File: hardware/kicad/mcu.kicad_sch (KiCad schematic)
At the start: 0 parts

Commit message: kicad: chunk #4 - MCU sub-sheet (ESP32-C6 SuperMini)
Populates mcu.kicad_sch with the ESP32-C6 SuperMini module
connector (U3), local 3.3V decoupling (C9 10uF + C9b 100nF),
and an unpopulated SWD/UART recovery header (J2, DNP).

ESP32-C6 SuperMini chosen per v0.3 research: lowest average
WiFi-active current (~60mA) thanks to WiFi 6 TWT/OFDMA, 512KB
SRAM headroom for BLE-proxy, ESPHome 2026 standardized on C6
for BLE-proxy roles. Antenna edge points to 12:00 (case wall)
per the clock-face sector layout.

Pinout (per v0.3 ARCHITECTURE.md, post strap-pin verification):
- GPIO 6 / 7: I2C SDA / SCL (shared bus, SEN66 + VEML7700 + NFC)
- GPIO 16 / 17: UART TX / RX (to LD2410 @ 256000 baud)
- GPIO 10: LD2410 OUT presence interrupt (was GPIO 4 - MTMS strap)
- GPIO 11: NFC FD interrupt (was GPIO 5 - MTDI strap)
- GPIO 8: onboard WS2812 status LED (no external WS2812 in v1)
- EN, GPIO 9: exposed on J2 recovery header

No external USB-C connector - flashing uses the SuperMini's own
onboard USB-C accessible before the enclosure is sealed. OTA via
ESPHome+HA handles all post-deployment updates.

J2 (SWD/UART recovery header, 6 pins) is marked DNP - footprint
exists on PCB for emergency hand-soldering if OTA fails, but is
not assembled by default.

Inter-sheet signals (I2C, UART, presence / NFC interrupts) are
exposed as hierarchical labels in mcu.kicad_sch and matching
sheet ports were preemptively added to oas.kicad_sch's MCU
sheet block, ready for the sensors sub-sheet (chunk #5).

Generator changes:
- New SUBSHEET_PINS dict + _gen_sheet_pin helper: declarative
  sheet port specification on the root sheet block.
- _gen_sheet_block rewritten without textwrap.dedent so the
  interpolated pin_block does not corrupt the leading whitespace
  pattern (fixes an indentation bug).
- _sch_capacitor and _sch_power_flag gained a sheet_key parameter
  (defaults to "power") so they can record the correct hierarchy
  path in their (instances ...) block when called from gen_mcu_sch.
- New hel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
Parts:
- added C9: 10uF 10V, symbol Device:C_Polarized
- added C9b: 100nF, symbol Device:C
- added J2: SWD/UART Recovery (DNP), symbol Connector_Generic:Conn_01x06
- added U3: ESP32-C6 SuperMini, symbol OAS:ESP32-C6_SuperMini
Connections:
- new net: J2.4 (Pin_4), U3.10 (GPIO9)
- new net: J2.3 (Pin_3), U3.9 (EN)
- new net +3V3: C9.1, C9b.1, J2.1 (Pin_1), U3.3 (3V3)
- new net GND: C9.2, C9b.2, J2.2 (Pin_2), U3.2 (GND)
- new net I2C_SCL: U3.5 (GPIO7)
- new net I2C_SDA: U3.4 (GPIO6)
- new net LD2410_OUT: U3.7 (GPIO10)
- new net NFC_FD: U3.8 (GPIO11)
- new net UART_RX: J2.6 (Pin_6), U3.12 (GPIO17)
- new net UART_TX: J2.5 (Pin_5), U3.11 (GPIO16)
- no-connect marks 0 -> 6

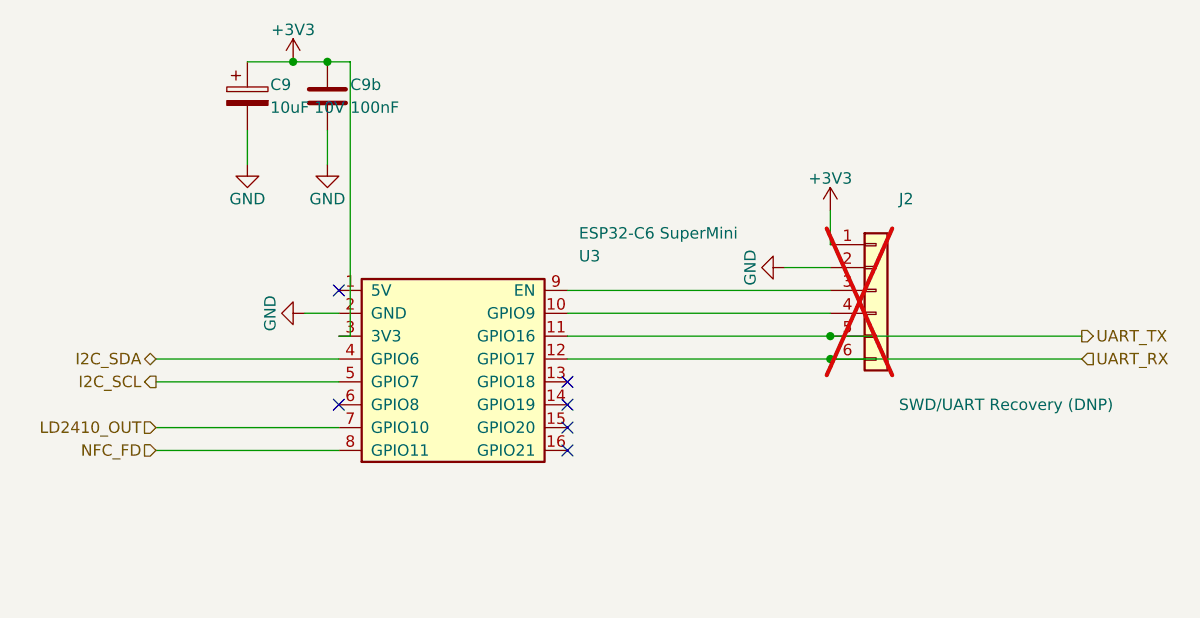
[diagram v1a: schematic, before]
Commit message: kicad: chunk #4 fix - J2 recovery header pinout (all 6 signals)
Fixes a layout bug in commit 2e83a5b: J2 (SWD/UART recovery,
DNP) had pin 1 left unconnected and the UART_RX wire passed
2.54 mm below J2 pin 6 without actually tapping into the
connector. A dangling junction at (194.31, 109.22) marked
where UART_RX should have entered but didn't. Net effect:
the recovery header was missing UART_RX, making it useless
for actual recovery flashing.

Refactored gen_mcu_sch() to map all 6 required recovery
signals into J2:
- Pin 1: +3V3   (programmer supplies power if needed)
- Pin 2: GND
- Pin 3: UART_TX (GPIO16)
- Pin 4: UART_RX (GPIO17)
- Pin 5: EN (reset)
- Pin 6: GPIO9 (BOOT mode)

Removed the dangling junction. No topology change in any
electrical net - all signals exist as before, only J2's
tapping points moved.

ERC and DRC unchanged. Generation deterministic.

Co-Authored-By: Claude Opus 4.7 (1M context) <noreply@anthropic.com>
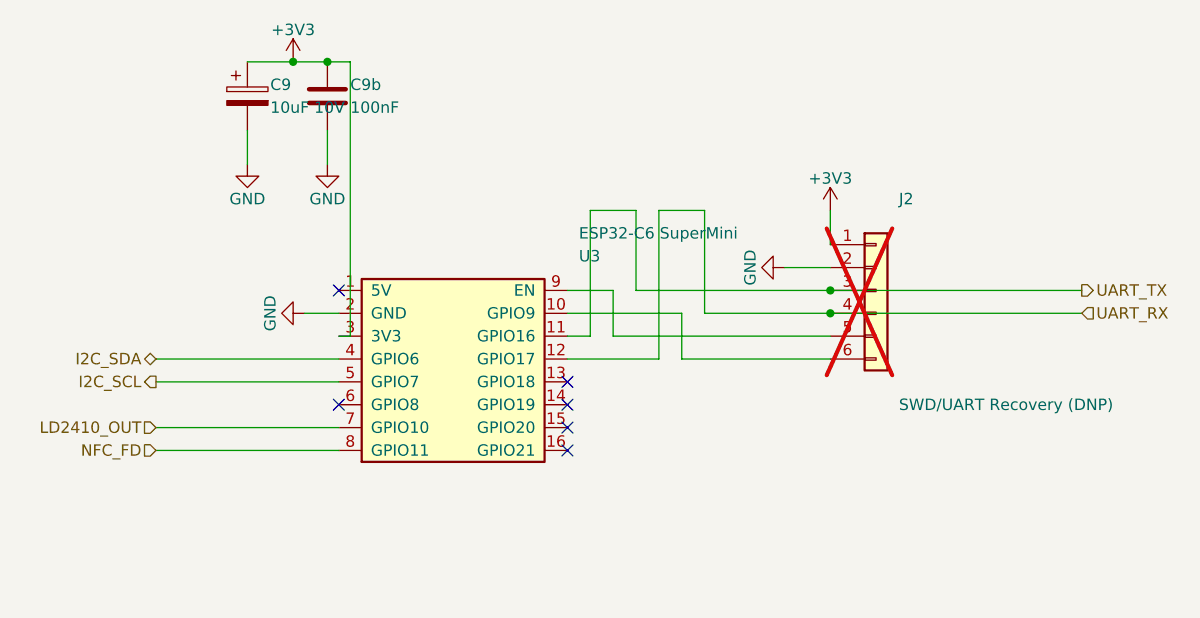
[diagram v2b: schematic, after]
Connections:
- net UART_RX: now also J2.4 (Pin_4); no longer J2.6 (Pin_6)
- net UART_TX: now also J2.3 (Pin_3); no longer J2.5 (Pin_5)
- net at U3.10 (GPIO9): now also J2.6 (Pin_6); no longer J2.4 (Pin_4)
- net at U3.9 (EN): now also J2.5 (Pin_5); no longer J2.3 (Pin_3)
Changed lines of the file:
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@@
 (wire
 	(pts
-		(xy 165.1 101.6) (xy 194.31 101.6)
-	)
-	(stroke
-		(width 0)
-		(type default)
-	)
-)
-(wire
-	(pts
-		(xy 165.1 104.14) (xy 194.31 104.14)
-	)
-	(stroke
-		(width 0)
-		(type default)
-	)
-)
-(wire
-	(pts
-		(xy 165.1 106.68) (xy 222.25 106.68)
-	)
-	(stroke
-		(width 0)
-		(type default)
-	)
-)
-(wire
-	(pts
-		(xy 165.1 109.22) (xy 222.25 109.22)
+		(xy 165.1 101.6) (xy 170.18 101.6)
+	)
+	(stroke
+		(width 0)
+		(type default)
+	)
+)
+(wire
+	(pts
+		(xy 170.18 101.6) (xy 170.18 106.68)
+	)
+	(stroke
+		(width 0)
+		(type default)
+	)
+)
+(wire
+	(pts
+		(xy 170.18 106.68) (xy 194.31 106.68)
+	)
+	(stroke
+		(width 0)
+		(type default)
+	)
+)
+(wire
+	(pts
+		(xy 165.1 104.14) (xy 177.8 104.14)
+	)
+	(stroke
+		(width 0)
+		(type default)
+	)
+)
+(wire
+	(pts
+		(xy 177.8 104.14) (xy 177.8 109.22)
+	)
+	(stroke
+		(width 0)
+		(type default)
+	)
+)
+(wire
+	(pts
+		(xy 177.8 109.22) (xy 194.31 109.22)
+	)
+	(stroke
+		(width 0)
+		(type default)
+	)
+)
+(wire
+	(pts
+		(xy 165.1 106.68) (xy 167.64 106.68)
+	)
+	(stroke
+		(width 0)
+		(type default)
+	)
+)
+(wire
+	(pts
+		(xy 167.64 106.68) (xy 167.64 92.71)
+	)
+	(stroke
+		(width 0)
+		(type default)
+	)
+)
+(wire
+	(pts
+		(xy 167.64 92.71) (xy 172.72 92.71)
+	)
+	(stroke
+		(width 0)
+		(type default)
+	)
+)
+(wire
+	(pts
+		(xy 172.72 92.71) (xy 172.72 101.6)
+	)
+	(stroke
+		(width 0)
+		(type default)
+	)
+)
+(wire
+	(pts
+		(xy 172.72 101.6) (xy 222.25 101.6)
 	)
 	(stroke
@@
 )
 (junction
-	(at 194.31 106.68)
+	(at 194.31 101.6)
 	(diameter 0)
 	(color 0 0 0 0)
 )
+(wire
+	(pts
+		(xy 165.1 109.22) (xy 175.26 109.22)
+	)
+	(stroke
+		(width 0)
+		(type default)
+	)
+)
+(wire
+	(pts
+		(xy 175.26 109.22) (xy 175.26 92.71)
+	)
+	(stroke
+		(width 0)
+		(type default)
+	)
+)
+(wire
+	(pts
+		(xy 175.26 92.71) (xy 180.34 92.71)
+	)
+	(stroke
+		(width 0)
+		(type default)
+	)
+)
+(wire
+	(pts
+		(xy 180.34 92.71) (xy 180.34 104.14)
+	)
+	(stroke
+		(width 0)
+		(type default)
+	)
+)
+(wire
+	(pts
+		(xy 180.34 104.14) (xy 222.25 104.14)
+	)
+	(stroke
+		(width 0)
+		(type default)
+	)
+)
 (junction
-	(at 194.31 109.22)
+	(at 194.31 104.14)
 	(diameter 0)
 	(color 0 0 0 0)
@@
 (hierarchical_label "UART_TX"
 	(shape output)
-	(at 222.25 106.68 0)
+	(at 222.25 101.6 0)
 	(effects
 		(font
@@
 (hierarchical_label "UART_RX"
 	(shape input)
-	(at 222.25 109.22 0)
-	(effects
-		(font
+	(at 222.25 104.14 0)
+	(effects
+		(font

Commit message: kicad: chunk #4 fix - v0.4 pinout + I2C pullups + DevKitM-1 symbol rebuild
Replace the OAS:ESP32-C6_SuperMini custom symbol (modeled on a generic 2x8
SIP, 16 pins) with OAS:ESP32-C6_DevKitM-1, built from the Espressif official
user guide pin layout (2x15 SIP, 30 pins total, J1 left + J3 right). Symbol
description carries MPN, EAN, datasheet URL, and chip-level notes (SiP flash,
GPIO 10/11 not bonded, 22 GPIOs available).

Apply the v0.4 signal-routing corrections:
  * LD2410_OUT: GPIO 10 (does not exist on SiP flash) -> GPIO 2 (safe input)
  * NFC_FD:    GPIO 11 (does not exist on SiP flash) -> GPIO 3 (safe input)

Add the I2C pullups flagged HIGH by the chunk #4 review:
  * R5: 4.7k 1% 0402, SDA -> +3V3
  * R6: 4.7k 1% 0402, SCL -> +3V3
Both placed near U3.10/U3.11 (GPIO 6/7) where the bus originates.

Bump C9 from 10V to 16V (0402 derating margin per review feedback). C9b
(100nF decoupling) unchanged.

Single-source-of-truth pin tables: ESP32C6_DEVKITM1_PINS (30 entries),
ESP32C6_DEVKITM1_SIGNAL_PIN (OAS-signal -> pin number lookup), and
ESP32C6_DEVKITM1_NC_PINS (no-connect list). Helpers _esp32c6_devkitm1_
lib_symbol() and _mcu_pin_xy() consume these tables so the schematic
mirrors the typed data — any future pinout change is a one-edit fix.

_sch_resistor() now takes a sheet_key parameter (default "power") so the
MCU sheet can pass "mcu" for its pullups. _sch_local_label() added for
short cross-body labels (RST, BOOT) connecting U3 to recovery header J2.

Determinism verified: two consecutive python generate.py runs produce
bit-identical mcu.kicad_sch (md5 d9e8810d7d465f22a01b8bd12c89970c).

DRC: 0 violations. ERC: 9 messages (6 errors + 3 warnings) -- all expected
incremental-build artifacts (hier labels I2C_SDA/SCL/LD2410_OUT/NFC_FD/
UART_TX/UART_RX waiting for sensors.kicad_sch and io.kicad_sch sheets to
declare matching pins). Two warnings dropped vs v0.5 baseline because the
I2C pullups now give SDA/SCL a second connection point on the MCU sheet.

Co-Author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
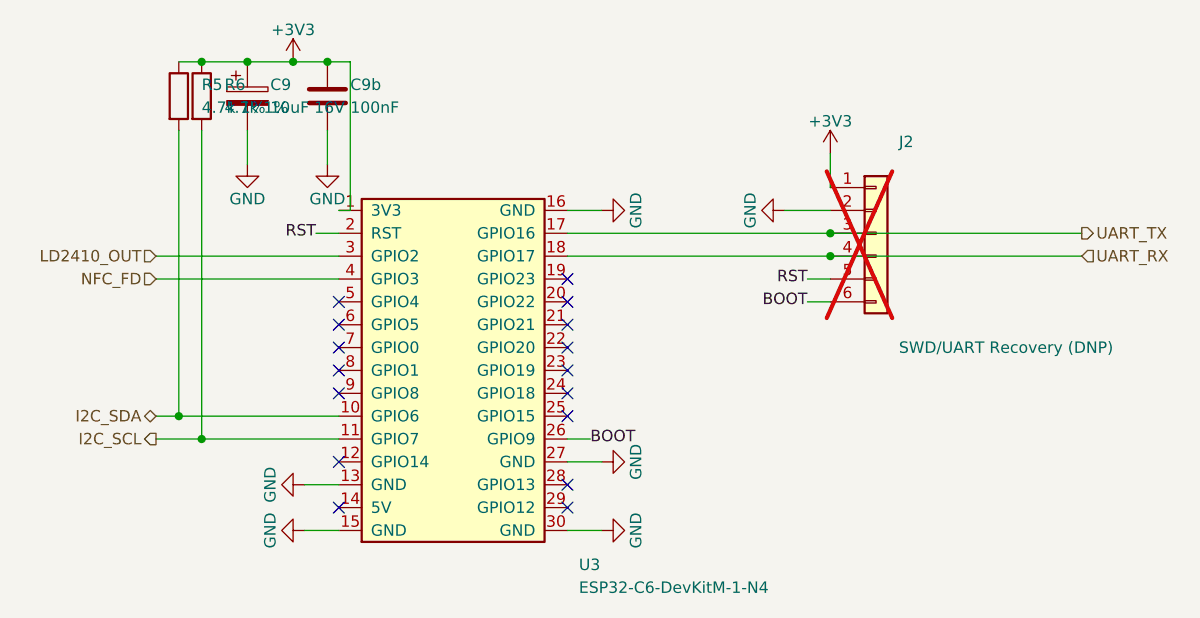
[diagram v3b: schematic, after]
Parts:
- removed U3: ESP32-C6 SuperMini, symbol OAS:ESP32-C6_SuperMini
- added R5, R6: 4.7k 1%, symbol Device:R
- added U3: ESP32-C6-DevKitM-1-N4, symbol OAS:ESP32-C6_DevKitM-1
- C9: value 10uF 10V -> 10uF 16V
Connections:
- net +3V3: now also R5.1, R6.1, U3.1 (3V3)
- net GND: now also U3.13 (GND), U3.15 (GND), U3.16 (GND), U3.27 (GND), U3.30 (GND)
- net I2C_SCL: now also R6.2, U3.11 (GPIO7)
- net I2C_SDA: now also R5.2, U3.10 (GPIO6)
- net LD2410_OUT: now also U3.3 (GPIO2)
- net NFC_FD: now also U3.4 (GPIO3)
- net UART_RX: now also U3.18 (GPIO17)
- net UART_TX: now also U3.17 (GPIO16)
- net BOOT: now reaches J2.6 (Pin_6)
- net BOOT: now also U3.26 (GPIO9)
- net RST: now reaches J2.5 (Pin_5)
- net RST: now also U3.2 (RST)
- no-connect marks 6 -> 16

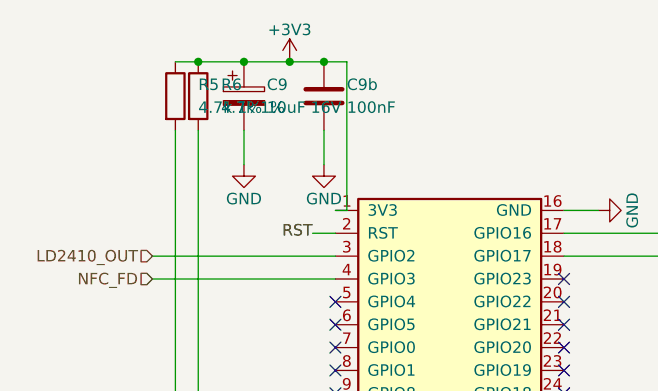
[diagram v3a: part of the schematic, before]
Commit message: docs+kicad: v0.6 - SEN66 moves to PCB + I2C pullup 4.7k->10k
Architectural reversal: SEN66 mounts directly on the PCB inside the
enclosure (no longer on the cover via JST-GH cable). Air-side face
points UP toward the AK-N-94 perforated cover; back face flat on PCB.
Body sticks 21.5 mm above PCB. Lifts hard constraint #1 from 17 mm to
>=22 mm in the SEN66 zone -- regional limit per CASE-VERIFICATION
section 1 (likely peripheral-only DXF annotation).

Mechanical retention: 4 zip-tie NPTH holes in PCB along the long
edges of the SEN66 footprint, in two corridors that avoid the air
openings (positions extracted from Sensirion STEP files):
  Pair 1: X ~25 mm (between inlets at X<=18.22 and outlet at X>=32.03)
  Pair 2: X ~50 mm (between outlet at X<=52.77 and connector at X=55.2)
Exact positions land in chunk #5a.

I2C pullups R5/R6 changed from 4.7 k to 10 k per SEN66 datasheet
section 3.1 spec. Standard mode (100 kHz) fully compatible; 6-device
bus + <50 mm trace fits well within rise-time budget. ESPHome default
50 kHz leaves comfortable margin.

Sensirion compliance notes recorded in CLAUDE.md v0.6 changelog:
  * Orientation: horizontal/lateral for wall-mount OAS = approved
  * 5 K over-temp budget (mech section 2.4, tcomp section 1)
  * Sealing divider REQUIRED between inlet zone and outlet zone
  * Do NOT thermally insulate the SEN66 body
  * STAR-Engine parameters are volatile - re-send on ESPHome boot
  * Recommended IAQM acceleration: T1=100, T2=300, K=20, P=20
  * VDD abs-max 3.6 V - TPS62933 margin holds
  * Fan resonances at 66.67 / 333.34 / 1000 Hz

Fallback recorded: if AK-N-94 physical verification fails 22 mm
clearance, escape to Combination Alpha (SPS30 + SCD41 + SGP41 + SHT45,
max 12 mm height, +EUR 20-30/unit, +4 ESPHome sensor blocks).

DRC: 0 violations. ERC: 9 messages, identical to v0.5 baseline (6
expected pin_not_connected errors + 3 warnings, all awaiting
sensors.kicad_sch / io.kicad_sch sheets).

Co-Authored-By: Claude Opus 4.7 (1M context) <no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
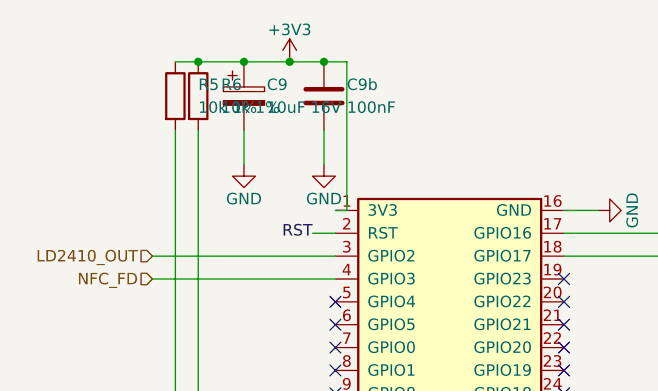
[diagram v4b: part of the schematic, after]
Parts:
- R5, R6: value 4.7k 1% -> 10k 1%
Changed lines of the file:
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@@
 		)
 	)
-	(property "Value" "4.7k 1%"
+	(property "Value" "10k 1%"
 		(at 124.46 81.28 0)
 		(effects
@@
 		)
 	)
-	(property "Value" "4.7k 1%"
+	(property "Value" "10k 1%"
 		(at 127 81.28 0)
 		(effects

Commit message: kicad+docs: v0.16 - AQI status LED ring (12 x SK6812-SIDE) + resolve OPEN ISSUE #2
Builds the side-emit RGB halo around the central cable hole: 12 SK6812 SIDE-A
LEDs on a Ø22 mm pitch circle (PCB origin = cable hole centre), each oriented
to emit radially OUTWARD into the AK-N-94 perforated cover. Per
hardware/components/_research-led-diffuse-ring.md the side-emit geometry
eliminates the "dot through perforation" problem at the structural level —
the cover never sees the die in line-of-sight.

Pinout verified twice (Normand SK6812 SIDE-A 2018 rev 01 + OPSCO SK6812
SIDE-A-001 2021 rev A/1, both via WebFetch + pdftotext): 1=DIN, 2=VDD,
3=DOUT, 4=GND. This differs from KiCad's stock LED:SK6812 symbol (which
is the PLCC4 5050 variant with 1=VSS/2=DIN/3=VDD/4=DOUT) — OAS ships its
own OAS:SK6812-SIDE symbol and oas:SK6812-SIDE footprint to avoid that
pitfall. Full part spec in hardware/components/sk6812-side.md.

Schematic additions (sensors.kicad_sch):
- 12 × D11..D22 OAS:SK6812-SIDE instances + 12 × C20..C31 Device:C 100 nF
  decoupling caps, vertical stack at X=40.64 with 25.4 mm row pitch.
- Daisy chain DIN→DOUT via 5-segment L-routes that bypass each LED body
  (avoids the spurious DIN↔DOUT short that a horizontal pass-through
  wire would create).
- D11 DIN driven from the new WS2812_DIN hierarchical label.
- D22 DOUT terminated with a no_connect.

Schematic / inter-sheet plumbing:
- mcu.kicad_sch: GPIO 8 (J1.9) moved from no-connect to signal pins.
  New WS2812_DIN hier label on the LEFT edge at the GPIO 8 pin row.
- SUBSHEET_PINS adds WS2812_DIN on the MCU and Sensors LEFT edges.
- Root sheet adds an inter-sheet wire at X = 41.91 (one grid step west
  of the existing NFC_FD vertical) joining the two new sheet pins.

PCB additions (oas.kicad_pcb):
- 12 × SK6812-SIDE footprints placed at θ = 0°..330° (30° steps) on the
  Ø22 mm pitch circle, each rotated to (270 - θ) so its body-local -Y
  (emission face) points radially outward.
- 12 × 100 nF 0402 caps, placed rad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
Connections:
- net WS2812_DIN: now reaches U3.9 (GPIO8)
- no-connect marks 16 -> 15
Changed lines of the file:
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@@
+(wire
+	(pts
+		(xy 139.7 113.03) (xy 119.38 113.03)
+	)
+	(stroke
+		(width 0)
+		(type default)
+	)
+)
 (wire
 	(pts
@@
 	)
 )
+(hierarchical_label "WS2812_DIN"
+	(shape output)
+	(at 119.38 113.03 180)
+	(effects
+		(font
+			(size 1.27 1.27)
+		)
+		(justify right)
+	)
+)
 (hierarchical_label "UART_TX"
 	(shape output)
@@
 )
 (no_connect
-	(at 139.7 113.03)
-)
-(no_connect
